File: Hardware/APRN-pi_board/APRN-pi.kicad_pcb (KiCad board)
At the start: 2 copper layers, 65 x 56.5 mm, 7 parts, among them J1 Raspberry_Pi_2_3, U1 DRA818V

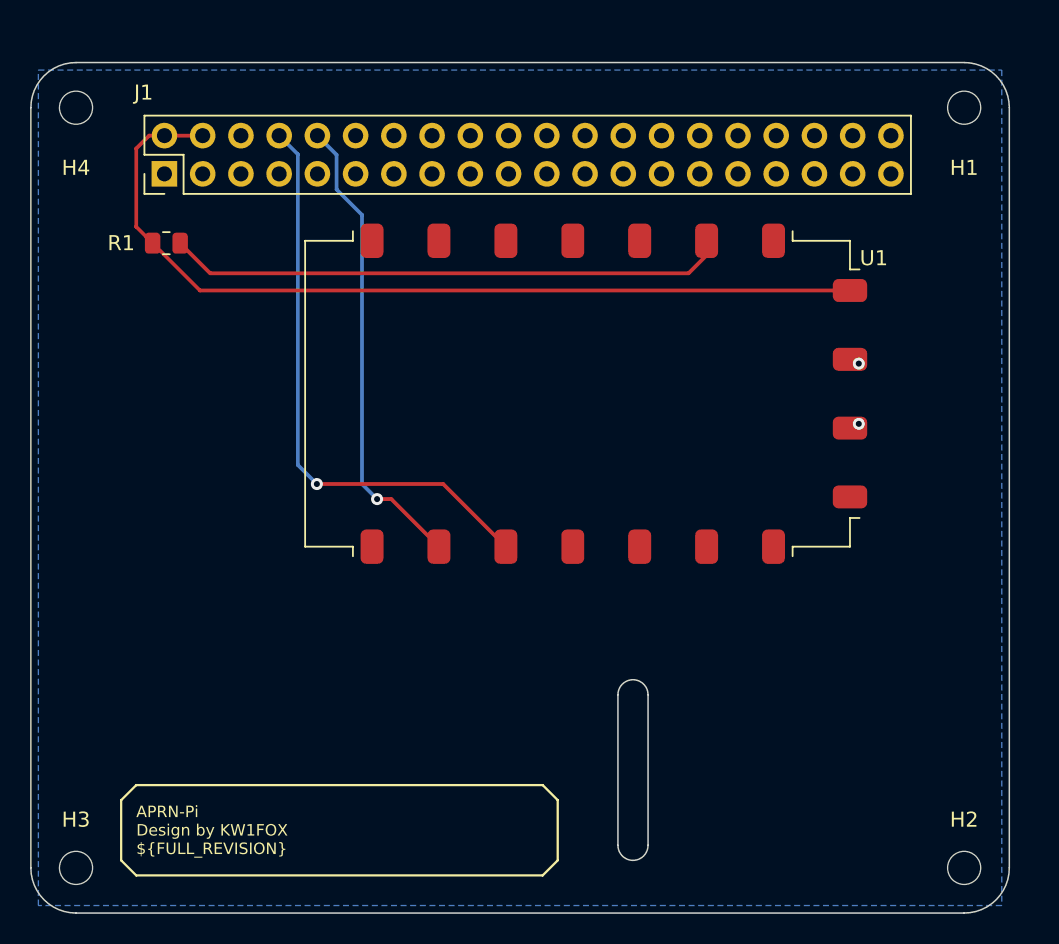
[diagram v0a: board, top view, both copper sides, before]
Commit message: Add RF components into schematic
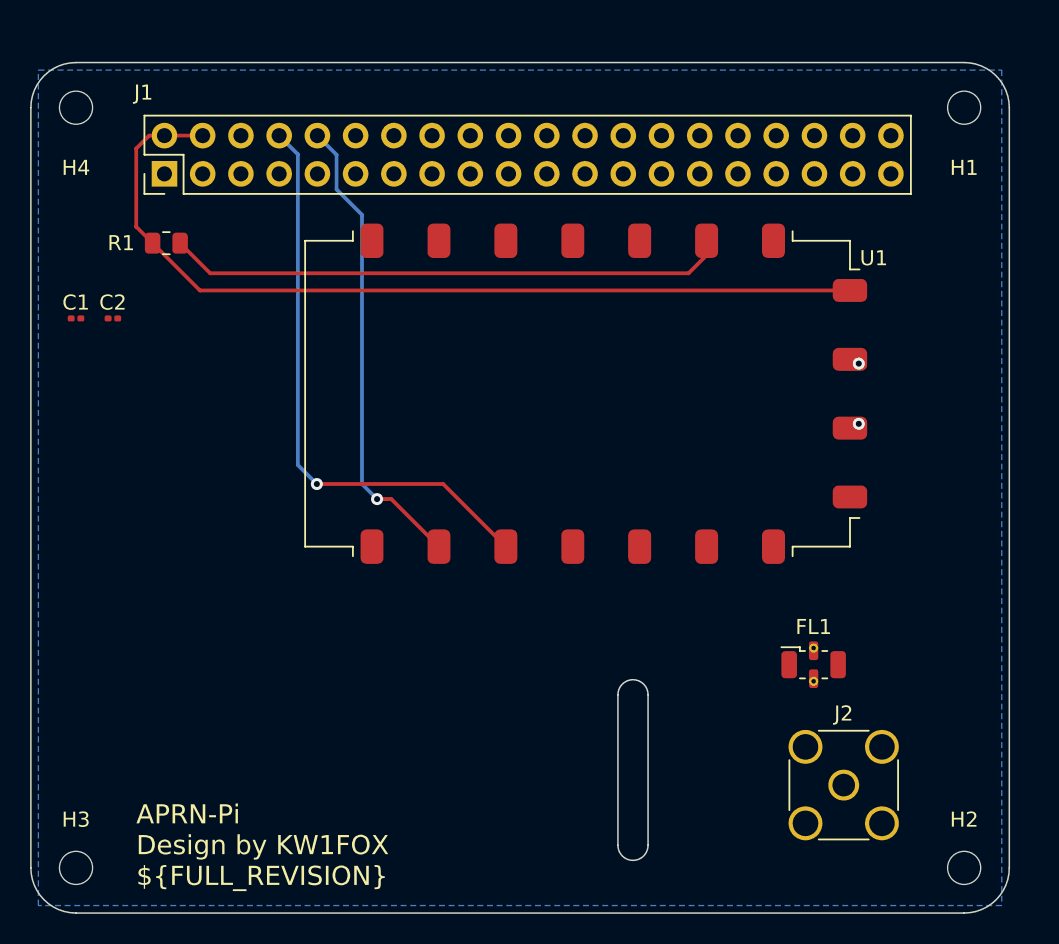
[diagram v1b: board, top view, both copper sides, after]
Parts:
- added C1: 100p, Capacitor_SMD:C_0201_0603Metric, F.Cu at (112.0, 82.0)
- added C2: 4.7u, Capacitor_SMD:C_0201_0603Metric, F.Cu at (114.5, 82.0)
- added FL1: LFCN-490, Filter:Filter_Mini-Circuits_FV1206, F.Cu at (161.0, 105.0)
- added J2: Conn_Coaxial, Connector_Coaxial:SMA_Amphenol_132291_Vertical, F.Cu at (163.0, 113.0)
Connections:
- U1 pad 12: unconnected-(U1-Pad12) -> ANT
- U1 pad 18: unconnected-(U1-Pad18) -> MIC
- U1 pad 5: unconnected-(U1-Pad5) -> PTT

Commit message: Bump to new logo and add logo
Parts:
- added L1: KITSUNE_LOGO, KenwoodFox:KITSUNE_LOGO, F.Cu at (118.0, 109.0)

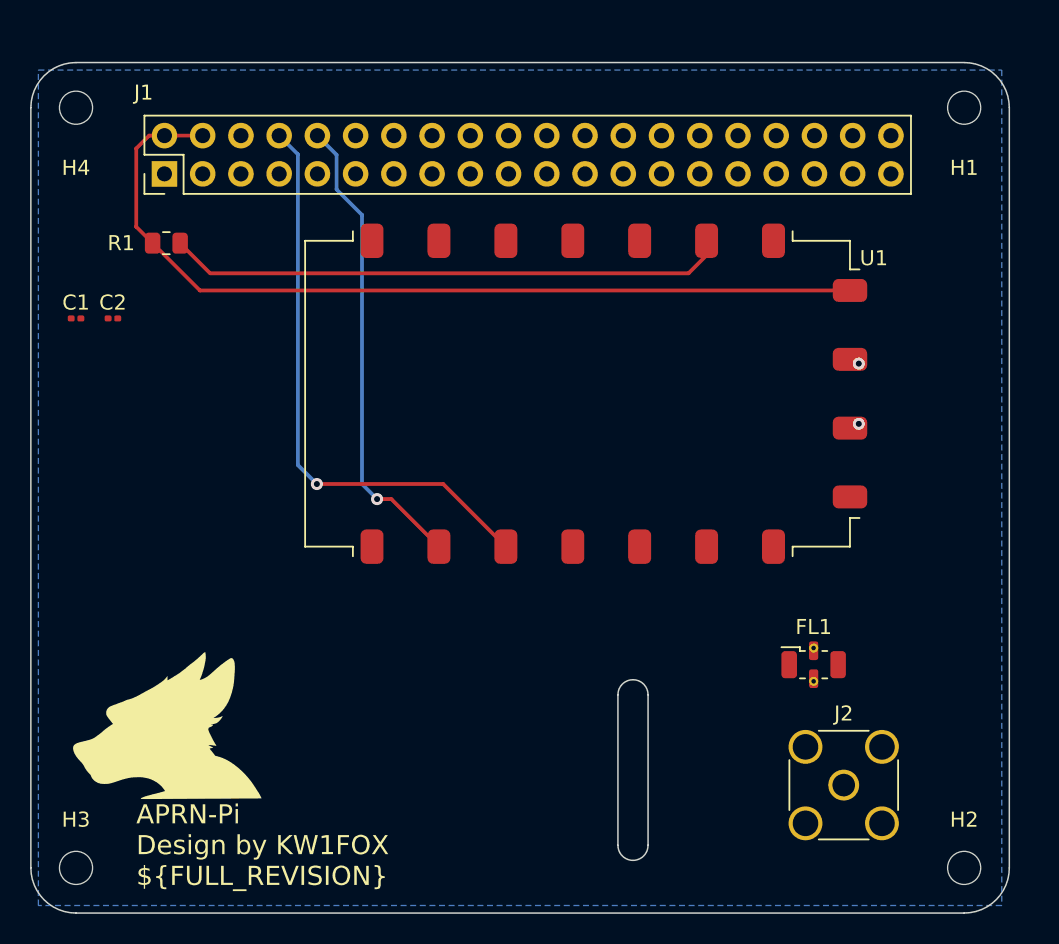
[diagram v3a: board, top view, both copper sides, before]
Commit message: Import last of dimms from pi
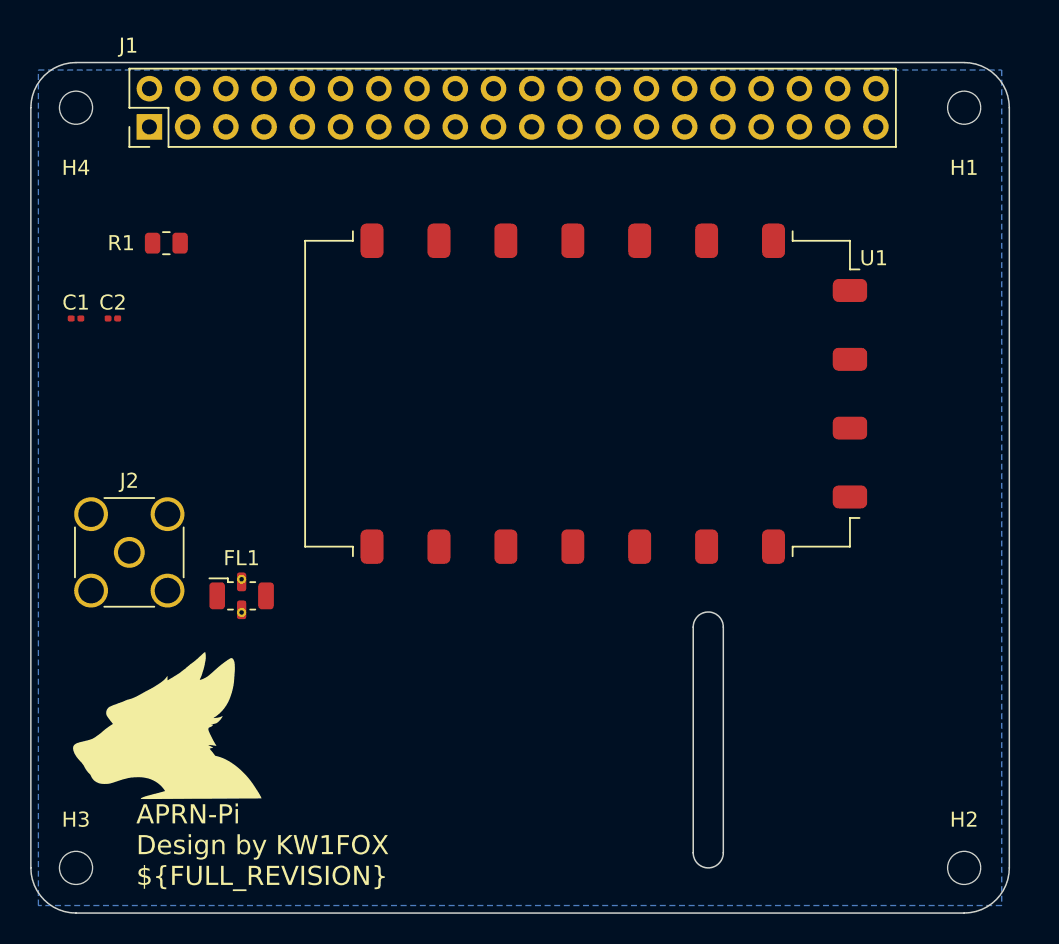
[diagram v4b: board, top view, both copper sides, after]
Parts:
- moved J2 49.9 mm to (115.5, 97.5)
- moved FL1 38.3 mm to (123.0, 100.4)
- moved J1 3.28 mm to (116.9, 69.3)
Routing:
- net +5V: track 59.1 -> 0.00 mm
- net TXD: track 38.5 -> 0.00 mm, vias 1 -> 0
- net Net-(R1-Pad1): track 37.3 -> 0.00 mm
- net RXD: track 31.2 -> 0.00 mm, vias 1 -> 0
- net GND: vias 2 -> 0
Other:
- outline, holes or cut-outs redrawn
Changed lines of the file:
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@@
   )
   (footprint "Filter:Filter_Mini-Circuits_FV1206" (layer "F.Cu")
-    (at 161 105)
+    (at 123 100.4275)
     (descr "Mini-Circuits Filter SMD 1206 https://ww2.minicircuits.com/case_style/FV1206.pdf")
     (tags "Mini-Circuits Filter SMD 1206")
@@
       (effects (font (size 1 1) (thickness 0.15)))
     )
-    (fp_text value "LFCN-490" (at 0 2.5) (layer "F.Fab")
+    (fp_text value "LFCN-490" (at 1 2.5725) (layer "F.Fab")
       (effects (font (size 1 1) (thickness 0.15)))
     )
@@
   )
   (footprint "Connector_PinHeader_2.54mm:PinHeader_2x20_P2.54mm_Vertical" (layer "F.Cu")
-    (at 117.875 72.395 90)
+    (at 116.875 69.275 90)
     (descr "Through hole straight pin header, 2x20, 2.54mm pitch, double rows")
     (tags "Through hole pin header THT 2x20 2.54mm double row")
@@
   )
   (footprint "Connector_Coaxial:SMA_Amphenol_132291_Vertical" (layer "F.Cu")
-    (at 163 113)
+    (at 115.54 97.54)
     (descr "https://www.amphenolrf.com/downloads/dl/file/id/3222/product/2918/132291_customer_drawing.pdf")
     (tags "SMA THT Female Jack Vertical Bulkhead")
@@
       (effects (font (size 1 1) (thickness 0.15)))
     )
-    (fp_text value "Conn_Coaxial" (at 0 5) (layer "F.Fab")
+    (fp_text value "Conn_Coaxial" (at -1.54 4.96) (layer "F.Fab")
       (effects (font (size 1 1) (thickness 0.15)))
     )
@@
     )
   )
-  (gr_line (start 150 117) (end 150 107) (layer "Edge.Cuts") (width 0.1))
+  (gr_line (start 155 117.5) (end 155 102.5) (layer "Edge.Cuts") (width 0.1))
   (gr_arc (start 112 121.5) (mid 109.87868 120.62132) (end 109 118.5) (layer "Edge.Cuts") (width 0.1))
   (gr_arc (start 171 65) (mid 173.12132 65.87868) (end 174 68) (layer "Edge.Cuts") (width 0.1))
-  (gr_arc (start 148 107) (mid 149 106) (end 150 107) (layer "Edge.Cuts") (width 0.1))
-  (gr_line (start 148 107) (end 148 117) (layer "Edge.Cuts") (width 0.1))
+  (gr_arc (start 153 102.5) (mid 154 101.5) (end 155 102.5) (layer "Edge.Cuts") (width 0.1))
+  (gr_line (start 153 102.5) (end 153 117.5) (layer "Edge.Cuts") (width 0.1))
   (gr_arc (start 109 68) (mid 109.87868 65.87868) (end 112 65) (layer "Edge.Cuts") (width 0.1))
-  (gr_arc (start 150 117) (mid 149 118) (end 148 117) (layer "Edge.Cuts") (width 0.1))
+  (gr_arc (start 155 117.5) (mid 154 118.5) (end 153 117.5) (layer "Edge.Cuts") (width 0.1))
   (gr_line (start 174 68) (end 174 118.5) (layer "Edge.Cuts") (width 0.1))
   (gr_line (start 171 65) (end 112 65) (layer "Edge.Cuts") (width 0.1))
@@
     (style (thickness 0.15) (arrow_length 1.27) (text_position_mode 0) (extension_height 0.58642) (extension_offset 0.5) keep_text_aligned)
   )
-  (segment (start 116 70.71) (end 116 75.9125) (width 0.25) (layer "F.Cu") (net 11))
-  (segment (start 116.855 69.855) (end 116 70.71) (width 0.25) (layer "F.Cu") (net 11))
-  (segment (start 116 75.9125) (end 117.0875 77) (width 0.25) (layer "F.Cu") (net 11))
-  (segment (start 117.0875 77) (end 120.2295 80.142) (width 0.25) (layer "F.Cu") (net 11))
-  (segment (start 120.2295 80.142) (end 163.415 80.142) (width 0.25) (layer "F.Cu") (net 11))
-  (segment (start 117.875 69.855) (end 116.855 69.855) (width 0.25) (layer "F.Cu") (net 11))
-  (segment (start 120.415 69.855) (end 117.875 69.855) (width 0.25) (layer "F.Cu") (net 11))
-  (via (at 164 85) (size 0.8) (drill 0.4) (layers "F.Cu" "B.Cu") (net 12))
-  (via (at 164 89) (size 0.8) (drill 0.4) (layers "F.Cu" "B.Cu") (net 12))
-  (segment (start 136.395 93) (end 140.555 97.16) (width 0.25) (layer "F.Cu") (net 14))
-  (segment (start 128 93) (end 136.395 93) (width 0.25) (layer "F.Cu") (net 14))
-  (via (at 128 93) (size 0.8) (drill 0.4) (layers "F.Cu" "B.Cu") (net 14))
-  (segment (start 125.495 69.855) (end 126.74 71.1) (width 0.25) (layer "B.Cu") (net 14))
-  (segment (start 126.74 71.1) (end 126.74 91.74) (width 0.25) (layer "B.Cu") (net 14))
-  (segment (start 126.74 91.74) (end 128 93) (width 0.25) (layer "B.Cu") (net 14))
-  (segment (start 132.95 94) (end 136.11 97.16) (width 0.25) (layer "F.Cu") (net 16))
-  (segment (start 132 94) (end 132.95 94) (width 0.25) (layer "F.Cu") (net 16))
-  (via (at 132 94) (size 0.8) (drill 0.4) (layers "F.Cu" "B.Cu") (net 16))
-  (segment (start 129.31 73.43) (end 129.31 71.13) (width 0.25) (layer "B.Cu") (net 16))
-  (segment (start 131 75.12) (end 129.31 73.43) (width 0.25) (layer "B.Cu") (net 16))
-  (segment (start 131 93) (end 131 75.12) (width 0.25) (layer "B.Cu") (net 16))
-  (segment (start 129.31 71.13) (end 128.035 69.855) (width 0.25) (layer "B.Cu") (net 16))
-  (segment (start 132 94) (end 131 93) (width 0.25) (layer "B.Cu") (net 16))
-  (segment (start 153.89 77.80248) (end 153.89 76.84) (width 0.25) (layer "F.Cu") (net 18))
-  (segment (start 152.69248 79) (end 153.89 77.80248) (width 0.25) (layer "F.Cu") (net 18))
-  (segment (start 118.9125 77) (end 120.9125 79) (width 0.25) (layer "F.Cu") (net 18))
-  (segment (start 120.9125 79) (end 152.69248 79) (width 0.25) (layer "F.Cu") (net 18))
+  (dimension (type aligned) (layer "F.Fab")
+    (pts (xy 109 115) (xy 154 115))
+    (height 13)
+    (gr_text "45.0000 mm" (at 131.5 126.85) (layer "F.Fab")
+      (effects (font (size 1 1) (thickness 0.15)))
+    )
+    (format (units 2) (units_format 1) (precision 4))
+    (style (thickness 0.1) (arrow_length 1.27) (text_position_mode 0) (extension_height 0.58642) (extension_offset 0.5) keep_text_aligned)
+  )
+  (dimension (type aligned) (layer "F.Fab")
+    (pts (xy 154 101.5) (xy 154 118.5))
+    (height 4.999999)
+    (gr_text "17.0000 mm" (at 147.850001 110 90) (layer "F.Fab")
+      (effects (font (size 1 1) (thickness 0.15)))
+    )
+    (format (units 2) (units_format 1) (precision 4))
+    (style (thickness 0.1) (arrow_length 1.27) (text_position_mode 0) (extension_height 0.58642) (extension_offset 0.5) keep_text_aligned)
+  )
+  (dimension (type aligned) (layer "F.Fab")
+    (pts (xy 154 121.5) (xy 154 110))
+    (height -11)
+    (gr_text "11.5000 mm" (at 141.85 115.75 90) (layer "F.Fab")
+      (effects (font (size 1 1) (thickness 0.15)))
+    )
+    (format (units 2) (units_format 1) (precision 4))
+    (style (thickness 0.1) (arrow_length 1.27) (text_position_mode 0) (extension_height 0.58642) (extension_offset 0.5) keep_text_aligned)
+  )
+  (dimension (type aligned) (layer "F.Fab")
+    (pts (xy 112.000001 68.000001) (xy 141 68.045))
+    (height -10)
+    (gr_text "29.0000 mm" (at 126.517301 56.872513 359.9110968) (layer "F.Fab")
+      (effects (font (size 1 1) (thickness 0.15)))
+    )
+    (format (units 2) (units_format 1) (precision 4))
+    (style (thickness 0.1) (arrow_length 1.27) (text_position_mode 0) (extension_height 0.58642) (extension_offset 0.5) keep_text_aligned)
+  )
   (zone (net 12) (net_name "GND") (layer "B.Cu") (name "GND") (hatch edge 0.508)
     (connect_pads (clearance 0.508))

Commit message: Fix RF stuff with help from @Gandalf#1068
Co-Authored By: @ka2qfx
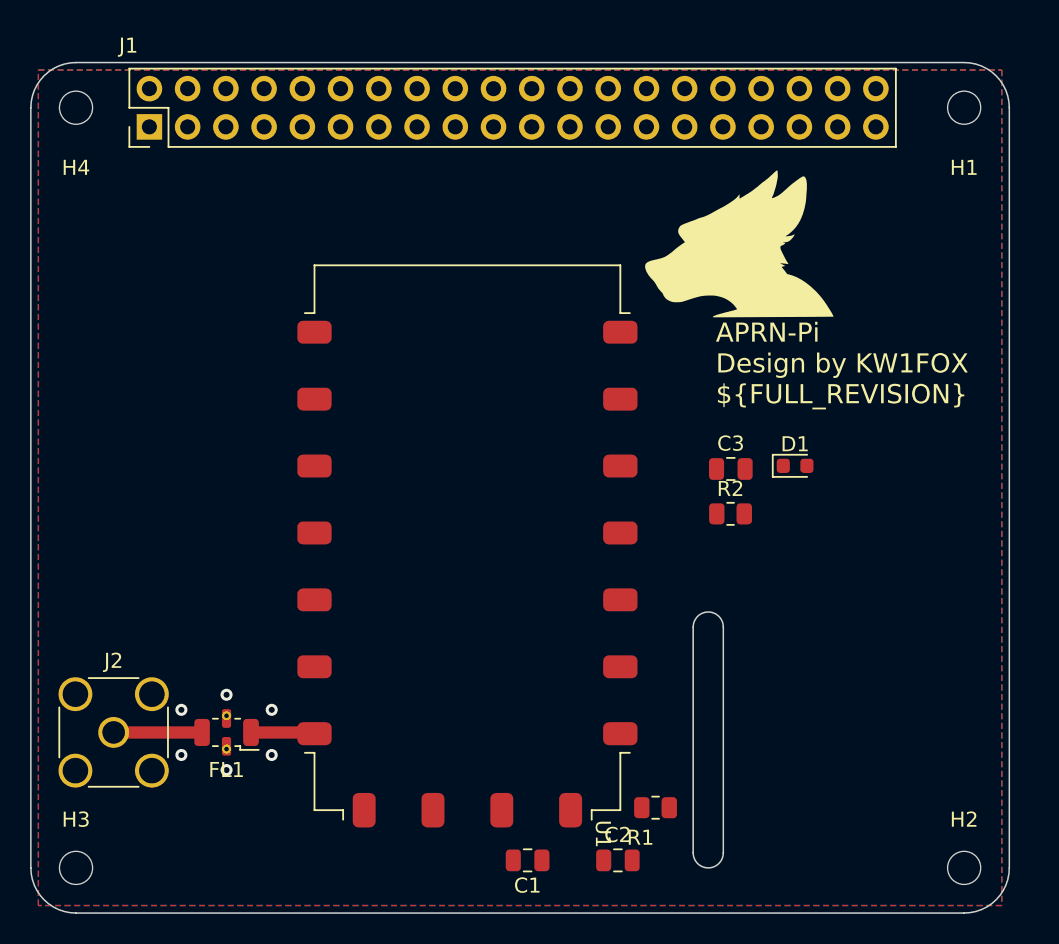
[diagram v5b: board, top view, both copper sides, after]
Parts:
- added C3: 1n, Capacitor_SMD:C_0805_2012Metric, F.Cu at (155.5, 92.0)
- added D1: DCD, LED_SMD:LED_0603_1608Metric, F.Cu at (159.8, 91.8)
- added R2: ?, Resistor_SMD:R_0805_2012Metric, F.Cu at (155.5, 95.0)
- C1, C2: footprint Capacitor_SMD:C_0201_0603Metric -> Capacitor_SMD:C_0805_2012Metric
- moved L1 49.7 mm to (156.0, 77.0)
- moved R1 49.6 mm to (150.5, 114.5)
- moved C2 49.2 mm to (148.0, 118.0)
- moved C1 46.9 mm to (142.0, 118.0), turned to 180 degrees
- moved J2 12.0 mm to (114.5, 109.5)
- moved U1 11.6 mm to (138.0, 96.2), turned to 0 degrees
- moved FL1 9.13 mm to (122.0, 109.5), turned to 180 degrees
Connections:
- J1 pad 1: unconnected-(J1-Pad1) -> +3V3
- J1 pad 17: unconnected-(J1-Pad17) -> +3V3
- J1 pad 18: unconnected-(J1-Pad18) -> Net-(J1-Pad18)
- J1 pad 22: unconnected-(J1-Pad22) -> PTT
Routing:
- net Net-(FL1-Pad3): track 0.00 -> 5.88 mm
- net ANT: track 0.00 -> 4.25 mm
- net GND: vias 0 -> 6
- added copper zone on F.Cu, net GND

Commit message: Even more fixups, thx!
Co-Authored By: @ka2qfx
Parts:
- added D1: RX, LED_SMD:LED_0603_1608Metric, F.Cu at (168.3, 94.0)
- added D3: TX, LED_SMD:LED_0603_1608Metric, F.Cu at (168.3, 90.0)
- added J3: Amplifier Jumper, Connector_PinHeader_2.54mm:PinHeader_1x03_P2.54mm_Vertical, F.Cu at (112.0, 100.0)
- added Q1: 2N3906, Package_TO_SOT_THT:TO-92_Inline, F.Cu at (112.0, 95.0)
- added R1: 180, Resistor_SMD:R_0805_2012Metric, F.Cu at (160.5, 94.0)
- added R3: 180, Resistor_SMD:R_0805_2012Metric, F.Cu at (160.5, 90.0)
- R2: value ? -> 180
- moved C3 12.8 mm to (151.0, 104.0), turned to -90 degrees
- moved D2 8.52 mm to (168.3, 92.0)
- moved R2 5.84 mm to (160.5, 92.0)
- moved R4 1.59 mm to (150.5, 112.9), turned to -90 degrees
- moved C1 0.75 mm to (142.0, 118.8)
- moved C2 0.75 mm to (148.0, 118.8)
- renumbered D1 to D2, R1 to R4
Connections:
- J1 pad 14: GND -> unconnected-(J1-Pad14)
- J1 pad 20: GND -> unconnected-(J1-Pad20)
- J1 pad 30: GND -> unconnected-(J1-Pad30)
- J1 pad 34: GND -> unconnected-(J1-Pad34)
- J1 pad 6: GND -> unconnected-(J1-Pad6)
- R2 pad 1: GND -> +3V3
- U1 pad 1: unconnected-(U1-Pad1) -> SQL
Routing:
- net +3V3: track 0.00 -> 82.6 mm, vias 0 -> 1
- net +5V: track 0.00 -> 81.2 mm
- net PTT: track 0.00 -> 71.4 mm
- net Net-(J1-Pad18): track 0.00 -> 56.2 mm
- net Net-(R3-Pad1): track 0.00 -> 48.5 mm, vias 0 -> 1
- net SQL: track 0.00 -> 31.7 mm
- net TXD: track 0.00 -> 27.4 mm, vias 0 -> 1
- net RXD: track 0.00 -> 22.5 mm, vias 0 -> 1
- net Net-(R3-Pad2): track 0.00 -> 8.32 mm
- net Net-(R2-Pad2): track 0.00 -> 8.32 mm
- net Net-(R1-Pad2): track 0.00 -> 8.32 mm
- net Net-(R4-Pad1): track 0.00 -> 7.83 mm
- net Net-(Q1-Pad3): track 0.00 -> 6.05 mm
